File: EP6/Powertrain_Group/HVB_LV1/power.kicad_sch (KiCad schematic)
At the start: 21 parts, among them U10 TPS5430DDAR

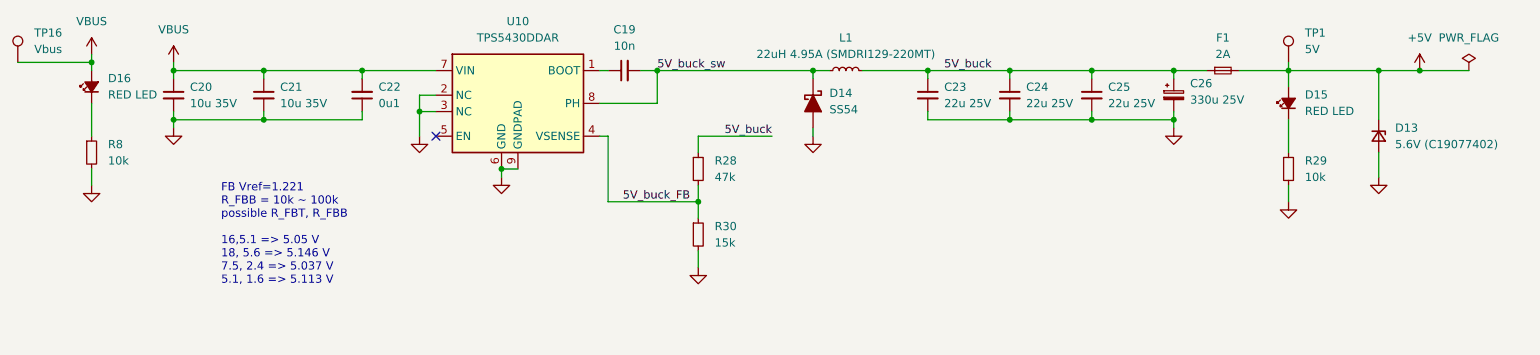
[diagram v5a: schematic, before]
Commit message: HVB_LV1 update to V3.1
V3.1 change to HV connector to JST 2.0 mm
     change power light to white
     add some RC filter to BSPD
     use CV buck instead of PWM dimmer + current control buck
     make RTML voltage not adjustable (12V)
     switch to 0805 for some LED
25/5/21 comment for FB1,FB2
CMI201209U2R2KT is 0805
GZ1608D601TF is 0603
should change layout or component
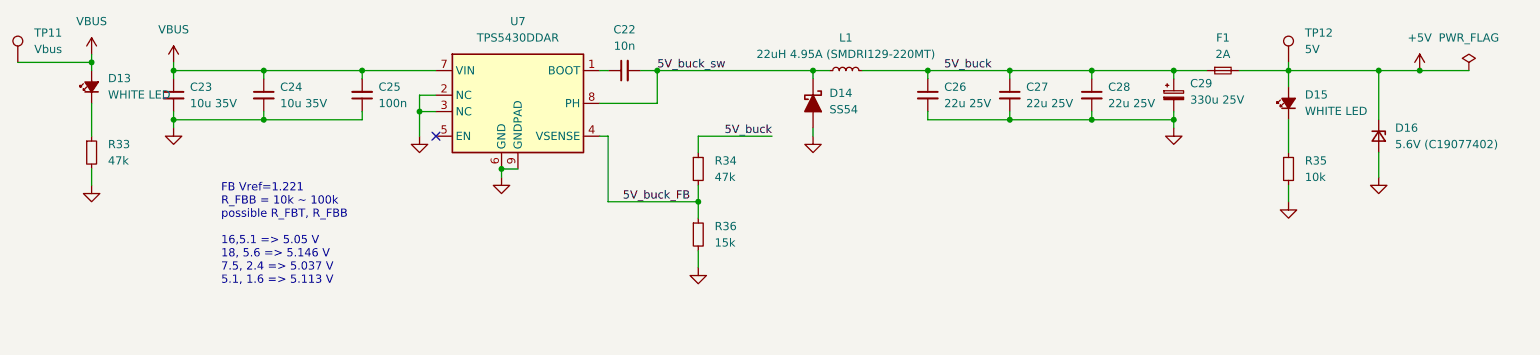
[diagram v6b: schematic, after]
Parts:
- C25: renamed from C22; value 0u1 -> 100n
- D13: renamed from D16; value RED LED -> WHITE LED
- D15: value RED LED -> WHITE LED
- R33: renamed from R8; value 10k -> 47k
- renumbered C19 to C22, C20 to C23, C21 to C24, C23 to C26, C24 to C27, C25 to C28, C26 to C29, D13 to D16, R28 to R34, R29 to R35, R30 to R36, TP16 to TP11, TP1 to TP12, U10 to U7
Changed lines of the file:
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@@
 	(title_block
 		(title "HVB_LV1")
-		(date "2025-03-19")
-		(rev "3.0")
+		(date "2025-05-18")
+		(rev "3.1")
 		(company "NTURacing")
 		(comment 1 "Powertrain")
@@
 		(on_board yes)
 		(dnp no)
-		(property "Reference" "C20"
+		(property "Reference" "C23"
 			(at 43.18 31.7562 0)
 			(effects
@@
 			(project "HVB_LV1"
 				(path "/e268df90-efd0-451f-9c39-af40eeef0439/8ccb6400-0ecc-48e8-87c6-ba8bc9bb1e9c"
-					(reference "C20")
+					(reference "C23")
 					(unit 1)
 				)
@@
 		(dnp no)
 		(fields_autoplaced yes)
-		(property "Reference" "#PWR097"
+		(property "Reference" "#PWR0100"
 			(at 227.33 52.07 0)
 			(effects
@@
 			(project "HVB_LV1"
 				(path "/e268df90-efd0-451f-9c39-af40eeef0439/8ccb6400-0ecc-48e8-87c6-ba8bc9bb1e9c"
-					(reference "#PWR097")
+					(reference "#PWR0100")
 					(unit 1)
 				)
@@
 		(dnp no)
 		(fields_autoplaced yes)
-		(property "Reference" "C22"
+		(property "Reference" "C25"
 			(at 72.39 31.7435 0)
 			(effects
@@
 			)
 		)
-		(property "Value" "0u1"
+		(property "Value" "100n"
 			(at 72.39 34.2835 0)
 			(effects
@@
 			(project "HVB_LV1"
 				(path "/e268df90-efd0-451f-9c39-af40eeef0439/8ccb6400-0ecc-48e8-87c6-ba8bc9bb1e9c"
-					(reference "C22")
+					(reference "C25")
 					(unit 1)
 				)
@@
 		(dnp no)
 		(fields_autoplaced yes)
-		(property "Reference" "U10"
+		(property "Reference" "U7"
 			(at 93.98 21.59 0)
 			(effects
@@
 			(project "HVB_LV1"
 				(path "/e268df90-efd0-451f-9c39-af40eeef0439/8ccb6400-0ecc-48e8-87c6-ba8bc9bb1e9c"
-					(reference "U10")
+					(reference "U7")
 					(unit 1)
 				)
@@
 		(dnp no)
 		(fields_autoplaced yes)
-		(property "Reference" "TP1"
+		(property "Reference" "TP12"
 			(at 215.9 23.368 0)
 			(effects
@@
 			(project "HVB_LV1"
 				(path "/e268df90-efd0-451f-9c39-af40eeef0439/8ccb6400-0ecc-48e8-87c6-ba8bc9bb1e9c"
-					(reference "TP1")
+					(reference "TP12")
 					(unit 1)
 				)
@@
 		(dnp no)
 		(fields_autoplaced yes)
-		(property "Reference" "#PWR03"
+		(property "Reference" "#PWR097"
 			(at 78.74 45.72 0)
 			(effects
@@
 			(project "HVB_LV1"
 				(path "/e268df90-efd0-451f-9c39-af40eeef0439/8ccb6400-0ecc-48e8-87c6-ba8bc9bb1e9c"
-					(reference "#PWR03")
+					(reference "#PWR097")
 					(unit 1)
 				)
@@
 		(dnp no)
 		(fields_autoplaced yes)
-		(property "Reference" "C24"
+		(property "Reference" "C27"
 			(at 172.72 31.7562 0)
 			(effects
@@
 			(project "HVB_LV1"
 				(path "/e268df90-efd0-451f-9c39-af40eeef0439/8ccb6400-0ecc-48e8-87c6-ba8bc9bb1e9c"
-					(reference "C24")
+					(reference "C27")
 					(unit 1)
 				)
@@
 		(dnp no)
 		(fields_autoplaced yes)
-		(property "Reference" "#PWR095"
+		(property "Reference" "#PWR093"
 			(at 40.64 31.75 0)
 			(effects
@@
 			(project "HVB_LV1"
 				(path "/e268df90-efd0-451f-9c39-af40eeef0439/8ccb6400-0ecc-48e8-87c6-ba8bc9bb1e9c"
-					(reference "#PWR095")
+					(reference "#PWR093")
 					(unit 1)
 				)
@@
 		(dnp no)
 		(fields_autoplaced yes)
-		(property "Reference" "#PWR0101"
+		(property "Reference" "#PWR099"
 			(at 91.44 52.07 0)
 			(effects
@@
 			(project "HVB_LV1"
 				(path "/e268df90-efd0-451f-9c39-af40eeef0439/8ccb6400-0ecc-48e8-87c6-ba8bc9bb1e9c"
-					(reference "#PWR0101")
+					(reference "#PWR099")
 					(unit 1)
 				)
@@
 		(dnp no)
 		(fields_autoplaced yes)
-		(property "Reference" "#PWR096"
+		(property "Reference" "#PWR094"
 			(at 233.68 33.02 0)
 			(effects
@@
 			(project "HVB_LV1"
 				(path "/e268df90-efd0-451f-9c39-af40eeef0439/8ccb6400-0ecc-48e8-87c6-ba8bc9bb1e9c"
-					(reference "#PWR096")
+					(reference "#PWR094")
 					(unit 1)
 				)
@@
 		(on_board yes)
 		(dnp no)
-		(property "Reference" "R30"
+		(property "Reference" "R36"
 			(at 124.46 53.34 0)
 			(effects
@@
 			(project "HVB_LV1"
 				(path "/e268df90-efd0-451f-9c39-af40eeef0439/8ccb6400-0ecc-48e8-87c6-ba8bc9bb1e9c"
-					(reference "R30")
+					(reference "R36")
 					(unit 1)
 				)
@@
 		(dnp no)
 		(fields_autoplaced yes)
-		(property "Reference" "#PWR0114"
+		(property "Reference" "#PWR092"
 			(at 27.94 30.48 0)
 			(effects
@@
 			(project "HVB_LV1"
 				(path "/e268df90-efd0-451f-9c39-af40eeef0439/8ccb6400-0ecc-48e8-87c6-ba8bc9bb1e9c"
-					(reference "#PWR0114")
+					(reference "#PWR092")
 					(unit 1)
 				)
@@
 		(dnp no)
 		(fields_autoplaced yes)
-		(property "Reference" "#PWR098"
+		(property "Reference" "#PWR096"
 			(at 195.58 44.45 0)
 			(effects
@@
 			(project "HVB_LV1"
 				(path "/e268df90-efd0-451f-9c39-af40eeef0439/8ccb6400-0ecc-48e8-87c6-ba8bc9bb1e9c"
-					(reference "#PWR098")
+					(reference "#PWR096")
 					(unit 1)
 				)
@@
 		(on_board yes)
 		(dnp no)
-		(property "Reference" "R28"
+		(property "Reference" "R34"
 			(at 124.46 43.18 0)
 			(effects
@@
 			(project "HVB_LV1"
 				(path "/e268df90-efd0-451f-9c39-af40eeef0439/8ccb6400-0ecc-48e8-87c6-ba8bc9bb1e9c"
-					(reference "R28")
+					(reference "R34")
 					(unit 1)
 				)
@@
 		(dnp no)
 		(fields_autoplaced yes)
-		(property "Reference" "C26"
+		(property "Reference" "C29"
 			(at 198.12 31.2038 0)
 			(effects
@@
 			(project "HVB_LV1"
 				(path "/e268df90-efd0-451f-9c39-af40eeef0439/8ccb6400-0ecc-48e8-87c6-ba8bc9bb1e9c"
-					(reference "C26")
+					(reference "C29")
 					(unit 1)
 				)
@@
 		(dnp no)
 		(fields_autoplaced yes)
-		(property "Reference" "D16"
-			(at 30.48 30.4165 90)
+		(property "Reference" "D13"
+			(at 30.48 30.4164 90)
 			(effects
 				(font
@@
 			)
 		)
-		(property "Value" "RED LED"
-			(at 30.48 32.9565 90)
+		(property "Value" "WHITE LED"
+			(at 30.48 32.9564 90)
 			(effects
 				(font
@@
 			(project "HVB_LV1"
 				(path "/e268df90-efd0-451f-9c39-af40eeef0439/8ccb6400-0ecc-48e8-87c6-ba8bc9bb1e9c"
-					(reference "D16")
+					(reference "D13")
 					(unit 1)
 				)
@@
 		(dnp no)
 		(fields_autoplaced yes)
-		(property "Reference" "C23"
+		(property "Reference" "C26"
 			(at 160.02 31.7562 0)
 			(effects
@@
 			(project "HVB_LV1"
 				(path "/e268df90-efd0-451f-9c39-af40eeef0439/8ccb6400-0ecc-48e8-87c6-ba8bc9bb1e9c"
-					(reference "C23")
+					(reference "C26")
 					(unit 1)
 				)
@@
 		(on_board yes)
 		(dnp no)
-		(property "Reference" "R29"
+		(property "Reference" "R35"
 			(at 215.9 43.18 0)
 			(effects
@@
 			(project "HVB_LV1"
 				(path "/e268df90-efd0-451f-9c39-af40eeef0439/8ccb6400-0ecc-48e8-87c6-ba8bc9bb1e9c"
-					(reference "R29")
+					(reference "R35")
 					(unit 1)
 				)
@@
 		(fields_autoplaced yes)
 		(property "Reference" "D15"
-			(at 215.9 32.9565 90)
+			(at 215.9 32.9564 90)
 			(effects
 				(font
@@
 			)
 		)
-		(property "Value" "RED LED"
-			(at 215.9 35.4965 90)
+		(property "Value" "WHITE LED"
+			(at 215.9 35.4964 90)
 			(effects
 				(font
@@
 		(dnp no)
 		(fields_autoplaced yes)
-		(property "Reference" "D13"
+		(property "Reference" "D16"
 			(at 229.87 38.1 90)
 			(effects
@@
 			(project "HVB_LV1"
 				(path "/e268df90-efd0-451f-9c39-af40eeef0439/8ccb6400-0ecc-48e8-87c6-ba8bc9bb1e9c"
-					(reference "D13")
+					(reference "D16")
 					(unit 1)
 				)
@@
 		(dnp no)
 		(fields_autoplaced yes)
-		(property "Reference" "C21"
+		(property "Reference" "C24"
 			(at 57.15 31.7562 0)
 			(effects
@@
 			(project "HVB_LV1"
 				(path "/e268df90-efd0-451f-9c39-af40eeef0439/8ccb6400-0ecc-48e8-87c6-ba8bc9bb1e9c"
-					(reference "C21")
+					(reference "C24")
 					(unit 1)
 				)
@@
 		(on_board yes)
 		(dnp no)
-		(property "Reference" "R8"
+		(property "Reference" "R33"
 			(at 30.48 40.64 0)
 			(effects
@@
 			)
 		)
-		(property "Value" "10k"
+		(property "Value" "47k"
 			(at 30.48 43.18 0)
 			(effects
@@
 			(project "HVB_LV1"
 				(path "/e268df90-efd0-451f-9c39-af40eeef0439/8ccb6400-0ecc-48e8-87c6-ba8bc9bb1e9c"
-					(reference "R8")
+					(reference "R33")
 					(unit 1)
 				)
@@
 		(dnp no)
 		(fields_autoplaced yes)
-		(property "Reference" "TP16"
+		(property "Reference" "TP11"
 			(at 19.05 23.368 0)
 			(effects
@@
 			(project "HVB_LV1"
 				(path "/e268df90-efd0-451f-9c39-af40eeef0439/8ccb6400-0ecc-48e8-87c6-ba8bc9bb1e9c"
-					(reference "TP16")
+					(reference "TP11")
 					(unit 1)
 				)
@@
 		(dnp no)
 		(fields_autoplaced yes)
-		(property "Reference" "#PWR0113"
+		(property "Reference" "#PWR0101"
 			(at 27.94 53.34 0)
 			(effects
@@
 			(project "HVB_LV1"
 				(path "/e268df90-efd0-451f-9c39-af40eeef0439/8ccb6400-0ecc-48e8-87c6-ba8bc9bb1e9c"
-					(reference "#PWR0113")
+					(reference "#PWR0101")
 					(unit 1)
 				)
@@
 		(dnp no)
 		(fields_autoplaced yes)
-		(property "Reference" "C19"
+		(property "Reference" "C22"
 			(at 110.4963 22.86 90)
 			(effects
@@
 			(project "HVB_LV1"
 				(path "/e268df90-efd0-451f-9c39-af40eeef0439/8ccb6400-0ecc-48e8-87c6-ba8bc9bb1e9c"
-					(reference "C19")
+					(reference "C22")
 					(unit 1)
 				)
@@
 		(dnp no)
 		(fields_autoplaced yes)
-		(property "Reference" "#PWR0100"
+		(property "Reference" "#PWR098"
 			(at 139.7 45.72 0)
 			(effects
@@
 			(project "HVB_LV1"
 				(path "/e268df90-efd0-451f-9c39-af40eeef0439/8ccb6400-0ecc-48e8-87c6-ba8bc9bb1e9c"
-					(reference "#PWR0100")
+					(reference "#PWR098")
 					(unit 1)
 				)
@@
 		(dnp no)
 		(fields_autoplaced yes)
-		(property "Reference" "C25"
+		(property "Reference" "C28"
 			(at 185.42 31.7562 0)
 			(effects
@@
 			(project "HVB_LV1"
 				(path "/e268df90-efd0-451f-9c39-af40eeef0439/8ccb6400-0ecc-48e8-87c6-ba8bc9bb1e9c"
-					(reference "C25")
+					(reference "C28")
 					(unit 1)
 				)
@@
 		(dnp no)
 		(fields_autoplaced yes)
-		(property "Reference" "#PWR099"
+		(property "Reference" "#PWR095"
 			(at 40.64 44.45 0)
 			(effects
@@
 			(project "HVB_LV1"
 				(path "/e268df90-efd0-451f-9c39-af40eeef0439/8ccb6400-0ecc-48e8-87c6-ba8bc9bb1e9c"
-					(reference "#PWR099")
+					(reference "#PWR095")
 					(unit 1)
 				)
